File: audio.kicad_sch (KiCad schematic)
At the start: 34 parts, among them IC10 LM386

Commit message: keyboard routing
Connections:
- net Left: now also R51.1; no longer R68.1
- net Right: now also R68.1; no longer R51.1
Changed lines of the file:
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@@
 	)
 	(label "Left"
+		(at 213.36 86.36 180)
+		(fields_autoplaced yes)
+		(effects
+			(font
+				(size 1.27 1.27)
+			)
+			(justify right bottom)
+		)
+	)
+	(label "Right"
 		(at 213.36 91.44 180)
 		(fields_autoplaced yes)
@@
 		(fields_autoplaced yes)
 		(effects
-			(font
-				(size 1.27 1.27)
-			)
-			(justify right bottom)
-		)
-	)
-	(label "Right"
-		(at 213.36 86.36 180)
-		(fields_autoplaced yes)
-		(effects

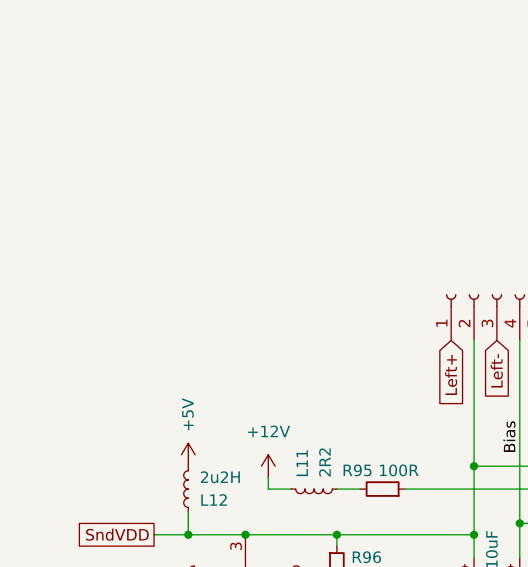
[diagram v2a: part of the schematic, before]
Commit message: fix footprint sizes
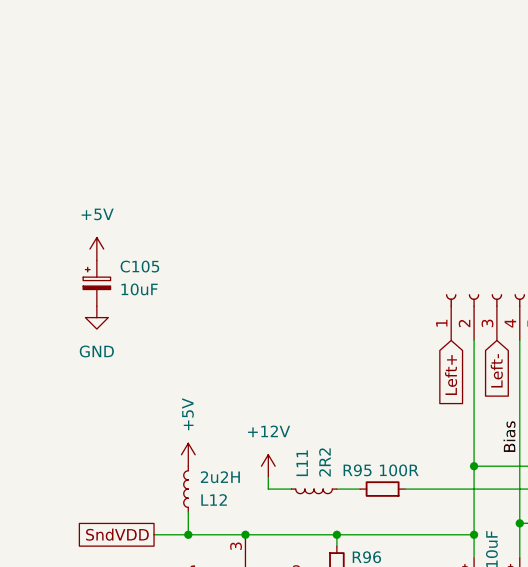
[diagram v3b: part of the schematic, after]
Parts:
- added C105: 10uF, Capacitor_THT:CP_Radial_Tantal_D7.0mm_P5.00mm, symbol Device:C_Polarized_Small
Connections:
- net +5V: now also C105.1
- net GND: now also C105.2
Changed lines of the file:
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@@
+	)
+	(symbol
+		(lib_id "Device:C_Polarized_Small")
+		(at 69.85 74.93 0)
+		(unit 1)
+		(exclude_from_sim no)
+		(in_bom yes)
+		(on_board yes)
+		(dnp no)
+		(fields_autoplaced yes)
+		(property "Reference" "C105"
+			(at 72.39 73.1138 0)
+			(effects
+				(font
+					(size 1.27 1.27)
+				)
+				(justify left)
+			)
+		)
+		(property "Value" "10uF"
+			(at 72.39 75.6538 0)
+			(effects
+				(font
+					(size 1.27 1.27)
+				)
+				(justify left)
+			)
+		)
+		(property "Footprint" "Capacitor_THT:CP_Radial_Tantal_D7.0mm_P5.00mm"
+			(at 69.85 74.93 0)
+			(effects
+				(font
+					(size 1.27 1.27)
+				)
+				(hide yes)
+			)
+		)
+		(property "Datasheet" "~"
+			(at 69.85 74.93 0)
+			(effects
+				(font
+					(size 1.27 1.27)
+				)
+				(hide yes)
+			)
+		)
+		(property "Description" "Polarized capacitor, small symbol"
+			(at 69.85 74.93 0)
+			(effects
+				(font
+					(size 1.27 1.27)
+				)
+				(hide yes)
+			)
+		)
+		(pin "2"
+		)
+		(pin "1"
+		)
+		(instances
+			(project "Acorn-A3010"
+				(path "/999882f3-94f8-4a89-9093-27a47d0cb289/0f9e4e4c-7eae-43dc-ad37-0c70003f4236"
+					(reference "C105")
+					(unit 1)
+				)
+			)
+		)
 	)
 	(symbol
@@
 	(symbol
 		(lib_id "power:GND")
+		(at 69.85 77.47 0)
+		(unit 1)
+		(exclude_from_sim no)
+		(in_bom yes)
+		(on_board yes)
+		(dnp no)
+		(fields_autoplaced yes)
+		(property "Reference" "#PWR0309"
+			(at 69.85 83.82 0)
+			(effects
+				(font
+					(size 1.27 1.27)
+				)
+				(hide yes)
+			)
+		)
+		(property "Value" "GND"
+			(at 69.85 82.55 0)
+			(effects
+				(font
+					(size 1.27 1.27)
+				)
+			)
+		)
+		(property "Footprint" ""
+			(at 69.85 77.47 0)
+			(effects
+				(font
+					(size 1.27 1.27)
+				)
+				(hide yes)
+			)
+		)
+		(property "Datasheet" ""
+			(at 69.85 77.47 0)
+			(effects
+				(font
+					(size 1.27 1.27)
+				)
+				(hide yes)
+			)
+		)
+		(property "Description" "Power symbol creates a global label with name \"GND\" , ground"
+			(at 69.85 77.47 0)
+			(effects
+				(font
+					(size 1.27 1.27)
+				)
+				(hide yes)
+			)
+		)
+		(pin "1"
+		)
+		(instances
+			(project "Acorn-A3010"
+				(path "/999882f3-94f8-4a89-9093-27a47d0cb289/0f9e4e4c-7eae-43dc-ad37-0c70003f4236"
+					(reference "#PWR0309")
+					(unit 1)
+				)
+			)
+		)
+	)
+	(symbol
+		(lib_id "power:GND")
 		(at 189.23 60.96 0)
 		(unit 1)
@@
 					(unit 1)
 				)
+			)
+		)
+	)
+	(symbol
+		(lib_id "power:+5V")
+		(at 69.85 72.39 0)
+		(unit 1)
+		(exclude_from_sim no)
+		(in_bom yes)
+		(on_board yes)
+		(dnp no)
+		(fields_autoplaced yes)
+		(property "Reference" "#PWR0308"
+			(at 69.85 76.2 0)
+			(effects
+				(font
+					(size 1.27 1.27)
+				)
+				(hide yes)
+			)
+		)
+		(property "Value" "+5V"
+			(at 69.85 67.31 0)
+			(effects
+				(font
+					(size 1.27 1.27)
+				)
+			)
+		)
+		(property "Footprint" ""
+			(at 69.85 72.39 0)
+			(effects
+				(font
+					(size 1.27 1.27)
+				)
+				(hide yes)
+			)
+		)
+		(property "Datasheet" ""
+			(at 69.85 72.39 0)
+			(effects
+				(font
+					(size 1.27 1.27)
+				)
+				(hide yes)
+			)
+		)
+		(property "Description" "Power symbol creates a global label with name \"+5V\""
+			(at 69.85 72.39 0)
+			(effects
+				(font
+					(size 1.27 1.27)
+				)
+				(hide yes)
+			)
+		)
+		(pin "1"
+		)
+		(instances
+			(project "Acorn-A3010"
+				(path "/999882f3-94f8-4a89-9093-27a47d0cb289/0f9e4e4c-7eae-43dc-ad37-0c70003f4236"
+					(reference "#PWR0308")
+					(unit 1)
+				)

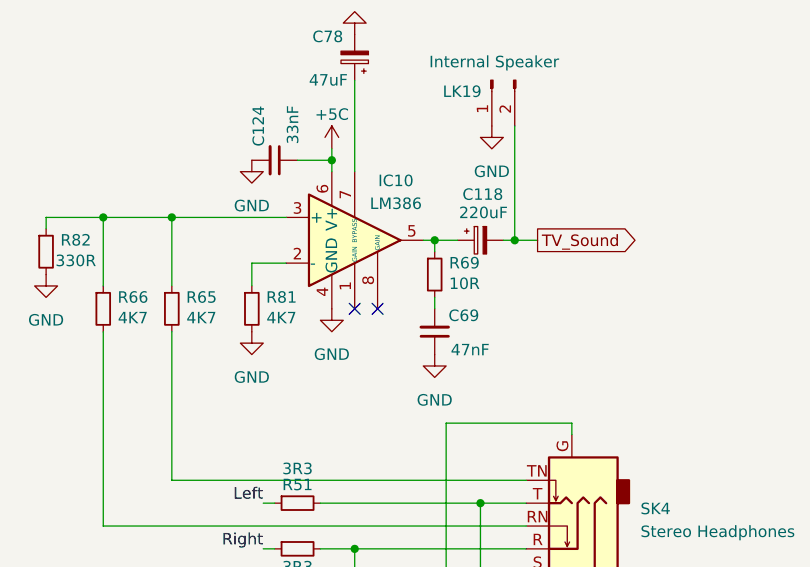
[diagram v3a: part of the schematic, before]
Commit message: adjust shielding perimeter trace and mounting holes
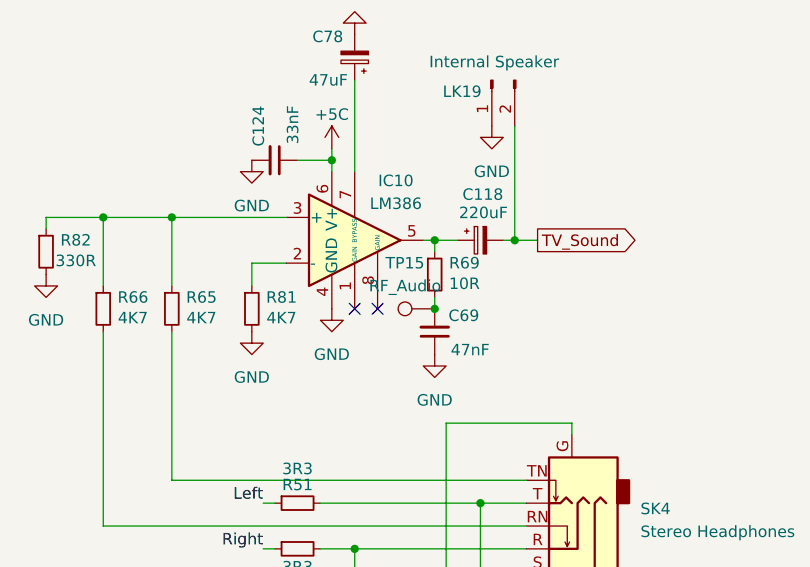
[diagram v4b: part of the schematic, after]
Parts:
- added TP15: RF_Audio, TestPoint:TestPoint_Pad_D1.0mm, symbol Connector:TestPoint
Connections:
- net at C69.2, R69.2: now also TP15.1
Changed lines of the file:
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@@
 	)
 	(junction
+		(at 232.41 64.77)
+		(diameter 0)
+		(color 0 0 0 0)
+	)
+	(junction
 		(at 132.08 121.92)
 		(diameter 0)
@@
 					(unit 1)
 				)
+			)
+		)
+	)
+	(symbol
+		(lib_id "Connector:TestPoint")
+		(at 232.41 64.77 90)
+		(unit 1)
+		(exclude_from_sim no)
+		(in_bom yes)
+		(on_board yes)
+		(dnp no)
+		(fields_autoplaced yes)
+		(property "Reference" "TP15"
+			(at 229.108 59.69 90)
+			(effects
+				(font
+					(size 1.27 1.27)
+				)
+			)
+		)
+		(property "Value" "RF_Audio"
+			(at 229.108 62.23 90)
+			(effects
+				(font
+					(size 1.27 1.27)
+				)
+			)
+		)
+		(property "Footprint" "TestPoint:TestPoint_Pad_D1.0mm"
+			(at 232.41 59.69 0)
+			(effects
+				(font
+					(size 1.27 1.27)
+				)
+				(hide yes)
+			)
+		)
+		(property "Datasheet" "~"
+			(at 232.41 59.69 0)
+			(effects
+				(font
+					(size 1.27 1.27)
+				)
+				(hide yes)
+			)
+		)
+		(property "Description" "test point"
+			(at 232.41 64.77 0)
+			(effects
+				(font
+					(size 1.27 1.27)
+				)
+				(hide yes)
+			)
+		)
+		(pin "1"
+		)
+		(instances
+			(project "Acorn-A3010"
+				(path "/999882f3-94f8-4a89-9093-27a47d0cb289/0f9e4e4c-7eae-43dc-ad37-0c70003f4236"
+					(reference "TP15")
+					(unit 1)
+				)

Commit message: add ide and rework onboard ram
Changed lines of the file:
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@@
 (kicad_sch
-	(version 20231120)
+	(version 20250114)
 	(generator "eeschema")
-	(generator_version "8.0")
+	(generator_version "9.0")
 	(paper "A4")
 	(junction
@@
 		)
 		(instances
-			(project ""
+			(project "Acorn-A3010"
 				(path "/999882f3-94f8-4a89-9093-27a47d0cb289/0f9e4e4c-7eae-43dc-ad37-0c70003f4236"
 					(reference "IM2")
@@
 		)
 		(instances
-			(project ""
+			(project "Acorn-A3010"
 				(path "/999882f3-94f8-4a89-9093-27a47d0cb289/0f9e4e4c-7eae-43dc-ad37-0c70003f4236"
 					(reference "IC10")
@@
 		)
 		(instances
-			(project ""
+			(project "Acorn-A3010"
 				(path "/999882f3-94f8-4a89-9093-27a47d0cb289/0f9e4e4c-7eae-43dc-ad37-0c70003f4236"
 					(reference "#PWR0179")
@@
 		)
 		(instances
-			(project ""
+			(project "Acorn-A3010"
 				(path "/999882f3-94f8-4a89-9093-27a47d0cb289/0f9e4e4c-7eae-43dc-ad37-0c70003f4236"
 					(reference "#PWR0296")
@@
 		)
 		(instances
-			(project ""
+			(project "Acorn-A3010"
 				(path "/999882f3-94f8-4a89-9093-27a47d0cb289/0f9e4e4c-7eae-43dc-ad37-0c70003f4236"
 					(reference "SK4")
